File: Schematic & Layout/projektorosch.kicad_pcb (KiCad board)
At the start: 2 copper layers, 39 parts, among them J1 Power barrel plug, J2 RJ12, U1 ATmega328-P, U2 MAX232, Y1 Crystal

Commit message: design pcb - first try
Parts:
- removed C1: 100nF, Capacitor_SMD:C_0805_2012Metric_Pad1.18x1.45mm_HandSolder
- removed R12: R, Resistor_SMD:R_0805_2012Metric_Pad1.20x1.40mm_HandSolder
- removed RESET1: SW_SPST, Button_Switch_SMD:SW_Push_1P1T_NO_6x6mm_H9.5mm
- D2: footprint Diode_SMD:D_0805_2012Metric_Pad1.15x1.40mm_HandSolder -> Diode_THT:D_DO-15_P2.54mm_Vertical_KathodeUp
- moved BTN2 123.6 mm to (120.0, 140.0)
- moved BTN1 117.9 mm to (120.0, 110.0)
- moved R3 100.7 mm to (130.0, 139.0), turned to -90 degrees
- moved J1 95.0 mm to (194.0, 103.0), turned to 180 degrees
- moved R6 86.0 mm to (113.2, 131.0), turned to 90 degrees
- moved R7 85.5 mm to (135.0, 139.0), turned to -90 degrees
- moved R1 83.3 mm to (129.0, 106.0), turned to 180 degrees
- moved R2 73.8 mm to (133.0, 111.0), turned to 90 degrees
- moved R10 69.8 mm to (162.0, 139.0), turned to -90 degrees
- moved R11 68.8 mm to (157.0, 139.0), turned to -90 degrees
- moved BTN4 68.4 mm to (170.2, 140.0)
- moved C9 67.8 mm to (153.3, 130.0), turned to 180 degrees
- moved R14 67.7 mm to (193.0, 131.5), turned to 90 degrees
- moved F1 66.7 mm to (187.4, 114.2), turned to 0 degrees
- moved C7 61.7 mm to (180.3, 102.5), turned to 0 degrees
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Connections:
- J2 pad 1: /RX -> GND
- J2 pad 3: GND -> /RX
- J2 pad 5: /RTS -> /CTS
- J2 pad 6: /CTS -> /RTS
- U1 pad 12: unconnected-(U1-Pad12) -> BTN1
- U1 pad 2: /TX -> Net-(U1-Pad2)
- U1 pad 21: Net-(C1-Pad1) -> unconnected-(U1-Pad21)
- U1 pad 23: BTN1 -> unconnected-(U1-Pad23)
- U1 pad 25: BTN3 -> unconnected-(U1-Pad25)
- U1 pad 28: unconnected-(U1-Pad28) -> Net-(D2-Pad2)
- U1 pad 6: Net-(D2-Pad2) -> BTN3
- U2 pad 12: /TX -> Net-(U1-Pad2)
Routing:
- net VCC: track 0.00 -> 310.1 mm, vias 0 -> 6
- net GND: track 0.00 -> 267.3 mm, vias 0 -> 8
- net Net-(D2-Pad2): track 0.00 -> 97.4 mm, vias 0 -> 1
- net /RTS: track 0.00 -> 64.3 mm
- net /CTS: track 0.00 -> 61.7 mm
- net /TX: track 0.00 -> 61.0 mm, vias 0 -> 1
- net /RX: track 0.00 -> 57.4 mm
- net !RESET: track 0.00 -> 32.5 mm, vias 0 -> 2
- net BTN4: track 0.00 -> 31.6 mm
- net BTN3: track 0.00 -> 26.2 mm
- net Net-(R6-Pad1): track 0.00 -> 24.6 mm
- net Net-(BTN1-Pad1): track 0.00 -> 20.4 mm
- net Net-(BTN2-Pad1): track 0.00 -> 19.9 mm
- net Net-(C8-Pad2): track 0.00 -> 19.1 mm
- net Net-(R4-Pad1): track 0.00 -> 18.1 mm
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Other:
- board outline added: 100 x 63 mm

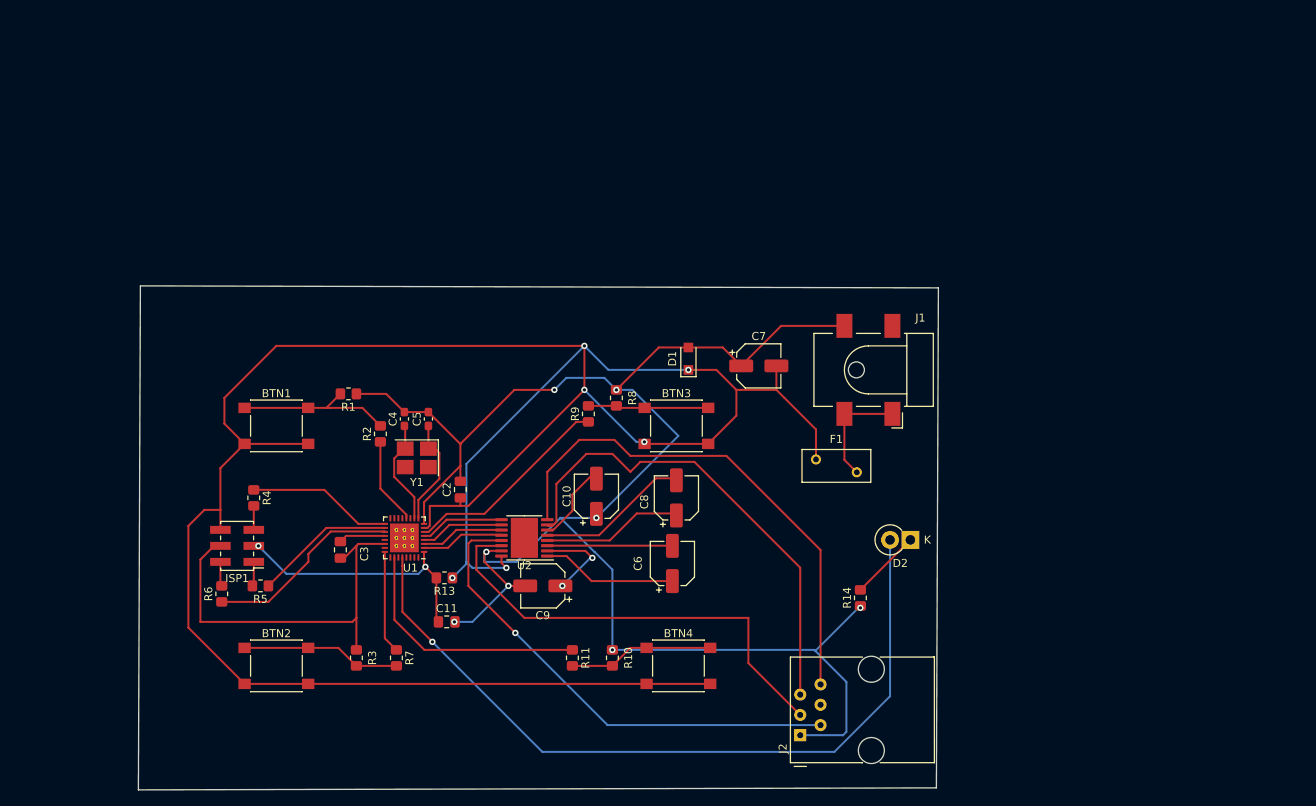
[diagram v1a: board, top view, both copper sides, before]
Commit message: redesign layout for attiny3216
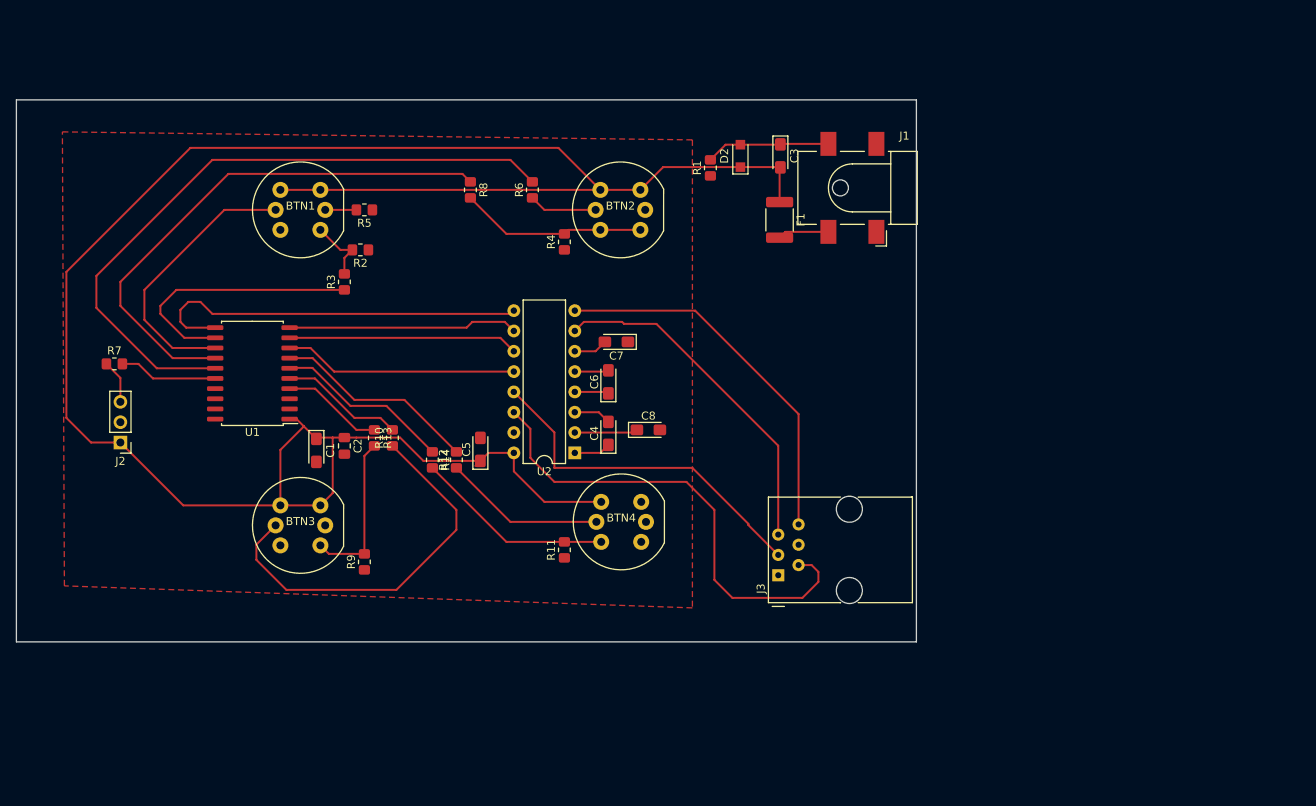
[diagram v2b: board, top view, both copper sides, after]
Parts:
- removed C10, C9: 10 uF, Capacitor_SMD:CP_Elec_5x5.7
- removed C11: 100nF, Capacitor_SMD:C_0805_2012Metric_Pad1.18x1.45mm_HandSolder
- removed D1: D_Zener 5.6V, Diode_SMD:Nexperia_CFP3_SOD-123W
- removed ISP1: Conn_02x03_Counter_Clockwise, Connector_PinHeader_2.00mm:PinHeader_2x03_P2.00mm_Vertical_SMD
- removed Y1: Crystal, Crystal:Crystal_SMD_3225-4Pin_3.2x2.5mm_HandSoldering
- added C1: 1u, Capacitor_Tantalum_SMD:CP_EIA-3216-10_Kemet-I_Pad1.58x1.35mm_HandSolder, F.Cu at (125.0, 113.1)
- added J3: RJ12, Connector_RJ:RJ12_Amphenol_54601, F.Cu at (182.7, 128.7)
- added R12: 220R, Resistor_SMD:R_0805_2012Metric_Pad1.20x1.40mm_HandSolder, F.Cu at (142.5, 114.2)
- BTN1: value ON_BTN -> LEDBTN; footprint Button_Switch_SMD:SW_Push_1P1T_NO_6x6mm_H9.5mm -> ledbtn_footprint:LBTN
- BTN2: value OFF_BTN -> LEDBTN; footprint Button_Switch_SMD:SW_Push_1P1T_NO_6x6mm_H9.5mm -> ledbtn_footprint:LBTN
- BTN3: value HDMI_BTN -> LEDBTN; footprint Button_Switch_SMD:SW_Push_1P1T_NO_6x6mm_H9.5mm -> ledbtn_footprint:LBTN
- BTN4: value VGA_BTN -> LEDBTN; footprint Button_Switch_SMD:SW_Push_1P1T_NO_6x6mm_H9.5mm -> ledbtn_footprint:LBTN
- C3: value 100n -> 10uF; footprint Capacitor_SMD:C_0805_2012Metric_Pad1.18x1.45mm_HandSolder -> Capacitor_Tantalum_SMD:CP_EIA-3216-12_Kemet-S_Pad1.58x1.35mm_HandSolder
- C4, C5: value 18p -> 1u; footprint Capacitor_SMD:C_0603_1608Metric_Pad1.08x0.95mm_HandSolder -> Capacitor_Tantalum_SMD:CP_EIA-3216-10_Kemet-I_Pad1.58x1.35mm_HandSolder
- C6, C8: value 10 uF -> 1u; footprint Capacitor_SMD:CP_Elec_5x5.7 -> Capacitor_Tantalum_SMD:CP_EIA-3216-10_Kemet-I_Pad1.58x1.35mm_HandSolder
- C7: value 10uF -> 1u; footprint Capacitor_SMD:CP_Elec_5x5.7 -> Capacitor_Tantalum_SMD:CP_EIA-3216-10_Kemet-I_Pad1.58x1.35mm_HandSolder
- D2: value LED -> D_Zener 5.6V; footprint Diode_THT:D_DO-15_P2.54mm_Vertical_KathodeUp -> Diode_SMD:Nexperia_CFP3_SOD-123W
- F1: footprint Fuse:Fuse_BelFuse_0ZRE0005FF_L8.3mm_W3.8mm -> Fuse:Fuse_1812_4532Metric_Pad1.30x3.40mm_HandSolder
- J2: value RJ12 -> Conn_01x03; footprint Connector_RJ:RJ12_Amphenol_54601 -> Connector_PinHeader_2.54mm:PinHeader_1x03_P2.54mm_Vertical
- R1: value 10K -> 0R
- R10: value 10K -> 220R
- R11, R2, R4, R9: value 100R -> 10K
- R13: value R -> 100R
- R14: value 220R -> 100R
- R3, R8: value 10K -> 100R
- R5, R6: value 100R -> 220R
- R7: value 100R -> 470R
- U1: value ATmega328-P -> ATtiny3216-S; footprint Package_DFN_QFN:QFN-32-1EP_5x5mm_P0.5mm_EP3.6x3.6mm_ThermalVias -> Package_SO:SOIC-20W_7.5x12.8mm_P1.27mm
- U2: footprint Package_SO:HTSSOP-16-1EP_4.4x5mm_P0.65mm_EP3.4x5mm_Mask2.46x2.31mm -> Package_DIP:DIP-16_W7.62mm
- moved J2 92.5 mm to (100.5, 112.1), turned to 180 degrees
- moved C3 73.8 mm to (183.0, 76.2)
- moved BTN2 71.4 mm to (163.0, 83.0)
- moved R6 63.7 mm to (152.0, 80.5)
- moved R14 56.2 mm to (139.5, 114.2), turned to -90 degrees
- moved R1 53.3 mm to (174.2, 77.8), turned to 90 degrees
- moved D2 52.5 mm to (178.0, 76.2), turned to 90 degrees
- moved R7 50.9 mm to (99.8, 102.2), turned to 0 degrees
- moved R4 50.3 mm to (156.0, 87.0), turned to 90 degrees
- moved R5 48.8 mm to (131.0, 83.0)
- moved BTN3 48.6 mm to (123.0, 122.4)
- moved R3 47.0 mm to (128.5, 92.0), turned to 90 degrees
- moved R10 38.9 mm to (134.5, 111.5), turned to 90 degrees
- moved R9 33.6 mm to (131.0, 127.0)
- moved R8 31.8 mm to (144.2, 80.5)
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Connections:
- BTN1 pad 1: Net-(BTN1-Pad1) -> VCC
- BTN1 pad 2: VCC -> Net-(BTN1-Pad2)
- BTN2 pad 1: Net-(BTN2-Pad1) -> VCC
- BTN2 pad 2: VCC -> Net-(BTN2-Pad2)
- BTN3 pad 1: Net-(BTN3-Pad1) -> VCC
- BTN3 pad 2: VCC -> Net-(BTN3-Pad2)
- BTN4 pad 1: Net-(BTN4-Pad1) -> VCC
- BTN4 pad 2: VCC -> Net-(BTN4-Pad2)
- C3 pad 1: VCC -> GND
- C3 pad 2: GND -> VCC
- C4 pad 2: GND -> Net-(C4-Pad2)
- C5 pad 1: Net-(C5-Pad1) -> VCC
- C7 pad 2: VCC -> Net-(C7-Pad2)
- C8 pad 2: Net-(C8-Pad2) -> GND
- D2 pad 1: Net-(D2-Pad1) -> VCC
- D2 pad 2: Net-(D2-Pad2) -> GND
- J2 pad 1: GND -> VCC
- J2 pad 2: /TX -> GND
- J2 pad 3: /RX -> Net-(J2-Pad3)
- R1 pad 2: Net-(BTN1-Pad1) -> GND
- R10 pad 1: GND -> Net-(BTN3-Pad3)
- R10 pad 2: Net-(BTN4-Pad1) -> BTN3LED
- R11 pad 1: BTN4 -> GND
- R11 pad 2: Net-(BTN4-Pad1) -> Net-(BTN4-Pad2)
- R13 pad 1: VCC -> BTN3
- R13 pad 2: !RESET -> Net-(BTN3-Pad2)
- R14 pad 1: GND -> BTN4
- R14 pad 2: Net-(D2-Pad1) -> Net-(BTN4-Pad2)
- R2 pad 1: BTN1 -> GND
- R2 pad 2: Net-(BTN1-Pad1) -> Net-(BTN1-Pad2)
- R3 pad 1: GND -> BTN1
- R3 pad 2: Net-(BTN2-Pad1) -> Net-(BTN1-Pad2)
- R4 pad 1: Net-(R4-Pad1) -> GND
- R4 pad 2: MOSI -> Net-(BTN2-Pad2)
- R5 pad 1: Net-(R5-Pad1) -> GND
- R5 pad 2: MISO -> Net-(BTN1-Pad4)
- R6 pad 1: Net-(R6-Pad1) -> Net-(BTN2-Pad3)
- R6 pad 2: SCK -> BTN2LED
- R7 pad 1: BTN2 -> Net-(J2-Pad3)
- R7 pad 2: Net-(BTN2-Pad1) -> UPDI
- R8 pad 1: GND -> BTN2
- R8 pad 2: Net-(BTN3-Pad1) -> Net-(BTN2-Pad2)
- R9 pad 1: BTN3 -> GND
- R9 pad 2: Net-(BTN3-Pad1) -> Net-(BTN3-Pad2)
- U1 pad 1: !RESET -> VCC
- U1 pad 10: Net-(C4-Pad1) -> CTSD
- U1 pad 11: unconnected-(U1-Pad11) -> RTSD
- U1 pad 13: unconnected-(U1-Pad13) -> BTN1LED
- U1 pad 14: unconnected-(U1-Pad14) -> BTN2
- U1 pad 15: unconnected-(U1-Pad15) -> BTN2LED
- U1 pad 16: unconnected-(U1-Pad16) -> UPDI
- U1 pad 17: Net-(R4-Pad1) -> unconnected-(U1-Pad17)
- U1 pad 18: Net-(R5-Pad1) -> unconnected-(U1-Pad18)
- U1 pad 19: Net-(R6-Pad1) -> unconnected-(U1-Pad19)
- U1 pad 2: Net-(U1-Pad2) -> unconnected-(U1-Pad2)
- U1 pad 20: VCC -> GND
- U1 pad 3: Net-(U1-Pad3) -> unconnected-(U1-Pad3)
- U1 pad 4: Net-(U1-Pad4) -> BTN3
- U1 pad 5: Net-(U1-Pad5) -> BTN3LED
- U1 pad 6: BTN3 -> BTN4
- U1 pad 7: VCC -> BTN4LED
- U1 pad 8: GND -> RXD
- U1 pad 9: Net-(C5-Pad1) -> TXD
- U2 pad 1: Net-(C6-Pad1) -> Net-(C4-Pad1)
- U2 pad 10: Net-(U1-Pad4) -> CTSD
- U2 pad 11: Net-(U1-Pad3) -> TXD
- U2 pad 12: Net-(U1-Pad2) -> RXD
- U2 pad 13: /TX -> RX
- U2 pad 14: /RX -> TX
- U2 pad 2: Net-(C9-Pad1) -> Net-(C8-Pad1)
- U2 pad 3: Net-(C6-Pad2) -> Net-(C4-Pad2)
- U2 pad 4: Net-(C8-Pad1) -> Net-(C6-Pad1)
- U2 pad 5: Net-(C8-Pad2) -> Net-(C6-Pad2)
- U2 pad 6: Net-(C10-Pad2) -> Net-(C7-Pad2)
- U2 pad 7: /CTS -> CTS
- U2 pad 8: /RTS -> RTS
- U2 pad 9: Net-(U1-Pad5) -> RTSD
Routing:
- net GND: track 267.3 -> 15.6 mm, vias 8 -> 0
- net Net-(D2-Pad2): track 97.4 -> 0.00 mm, vias 1 -> 0
- net BTN2LED: track 0.00 -> 83.6 mm
- net /RTS: track 64.3 -> 0.00 mm
- net /CTS: track 61.7 -> 0.00 mm
- net /TX: track 61.0 -> 0.00 mm, vias 1 -> 0
- net TX: track 0.00 -> 59.8 mm
- net /RX: track 57.4 -> 0.00 mm
- net BTN2: track 12.9 -> 67.3 mm
- net RTSD: track 0.00 -> 49.0 mm
- net Net-(BTN3-Pad3): track 0.00 -> 48.8 mm
- net RTS: track 0.00 -> 47.1 mm
- net VCC: track 310.1 -> 265.2 mm, vias 6 -> 0
- net RX: track 0.00 -> 44.2 mm
- net CTS: track 0.00 -> 43.4 mm
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- added copper zone on F.Cu, net GND
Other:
- board size 100 x 63 mm -> 112.5 x 67.8 mm

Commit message: attinty3216-remeljuk-final
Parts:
- removed D2: D_Zener 5.6V, Diode_SMD:Nexperia_CFP3_SOD-123W
- removed R1: 0R, Resistor_SMD:R_0805_2012Metric_Pad1.20x1.40mm_HandSolder
- removed R11, R4: 10K, Resistor_SMD:R_0805_2012Metric_Pad1.20x1.40mm_HandSolder
- removed R12, R6: 220R, Resistor_SMD:R_0805_2012Metric_Pad1.20x1.40mm_HandSolder
- removed R13, R14, R3: 100R, Resistor_SMD:R_0805_2012Metric_Pad1.20x1.40mm_HandSolder
- removed R7: 470R, Resistor_SMD:R_0805_2012Metric_Pad1.20x1.40mm_HandSolder
- added D1: D_Zener 5.6V, Diode_SMD:Nexperia_CFP3_SOD-123W, F.Cu at (176.8, 78.7)
- J1: value Power barrel plug -> Barrel_Jack_Switch; footprint Connector_BarrelJack:BarrelJack_CLIFF_FC681465S_SMT_Horizontal -> Connector_BarrelJack:BarrelJack_Horizontal
- R2, R9: value 10K -> 220R
- R8: value 100R -> 470R
- moved R8 31.5 mm to (123.1, 103.8), turned to 0 degrees
- moved R2 24.4 mm to (154.2, 82.3)
- moved C8 24.0 mm to (153.5, 90.3), turned to 90 degrees
- moved R5 20.1 mm to (123.1, 101.5), turned to 0 degrees
- moved J2 18.6 mm to (118.9, 109.0)
- moved R9 17.3 mm to (124.8, 110.9)
- moved U1 16.1 mm to (133.1, 103.3)
- moved R10 12.6 mm to (146.6, 107.7)
- moved C7 11.0 mm to (156.5, 90.3), turned to -90 degrees
- moved C3 9.47 mm to (173.9, 78.7), turned to 90 degrees
- moved C1 8.84 mm to (133.7, 114.7), turned to 180 degrees
- moved J1 6.00 mm to (186.0, 79.7)
- moved F1 5.81 mm to (180.7, 78.9)
- moved C2 5.62 mm to (134.1, 111.9), turned to 180 degrees
- moved C5 1.32 mm to (146.6, 112.1)
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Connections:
- BTN1 pad 1: VCC -> GND
- BTN1 pad 2: Net-(BTN1-Pad2) -> BTN1
- BTN1 pad 3: BTN1LED -> Net-(BTN1-Pad3)
- BTN1 pad 4: Net-(BTN1-Pad4) -> GND
- BTN2 pad 1: VCC -> GND
- BTN2 pad 2: Net-(BTN2-Pad2) -> BTN2
- BTN3 pad 1: VCC -> GND
- BTN3 pad 2: Net-(BTN3-Pad2) -> BTN3
- BTN4 pad 1: VCC -> GND
- BTN4 pad 2: Net-(BTN4-Pad2) -> BTN4
- J1 pad 3: (no net) -> GND
- R10 pad 1: Net-(BTN3-Pad3) -> Net-(BTN4-Pad3)
- R10 pad 2: BTN3LED -> BTN4LED
- R2 pad 1: GND -> Net-(BTN2-Pad3)
- R2 pad 2: Net-(BTN1-Pad2) -> BTN2LED
- R5 pad 1: GND -> Net-(BTN1-Pad3)
- R5 pad 2: Net-(BTN1-Pad4) -> BTN1LED
- R8 pad 1: BTN2 -> Net-(J2-Pad3)
- R8 pad 2: Net-(BTN2-Pad2) -> UPDI
- R9 pad 1: GND -> Net-(BTN3-Pad3)
- R9 pad 2: Net-(BTN3-Pad2) -> BTN3LED
- U1 pad 12: BTN1 -> BTN2
- U1 pad 13: BTN1LED -> BTN2LED
- U1 pad 14: BTN2 -> BTN1
- U1 pad 15: BTN2LED -> BTN1LED
- U1 pad 17: unconnected-(U1-Pad17) -> BTN3
- U1 pad 18: unconnected-(U1-Pad18) -> BTN3LED
- U1 pad 2: unconnected-(U1-Pad2) -> BTN4
- U1 pad 3: unconnected-(U1-Pad3) -> GND
- U1 pad 4: BTN3 -> GND
- U1 pad 5: BTN3LED -> BTN4LED
- U1 pad 6: BTN4 -> unconnected-(U1-Pad6)
- U1 pad 7: BTN4LED -> unconnected-(U1-Pad7)
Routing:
- net VCC: track 265.2 -> 177.1 mm
- net BTN2LED: track 83.6 -> 39.3 mm
- net Net-(BTN3-Pad3): track 48.8 -> 13.2 mm
- net BTN1LED: track 34.6 -> 4.90 mm
- net RTSD: track 49.0 -> 22.0 mm
- net Net-(BTN4-Pad2): track 24.9 -> 0.00 mm
- net Net-(BTN2-Pad2): track 23.3 -> 0.00 mm
- net BTN2: track 67.3 -> 46.8 mm
- net Net-(BTN1-Pad3): track 0.00 -> 20.3 mm
- net Net-(BTN3-Pad2): track 20.0 -> 0.00 mm
- net BTN3: track 12.7 -> 32.6 mm
- net CTSD: track 28.8 -> 12.2 mm
- net RXD: track 29.3 -> 13.2 mm
- net TXD: track 28.7 -> 12.7 mm
- net BTN4LED: track 25.7 -> 9.98 mm
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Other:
- board size 112.5 x 67.8 mm -> 92.3 x 67.8 mm

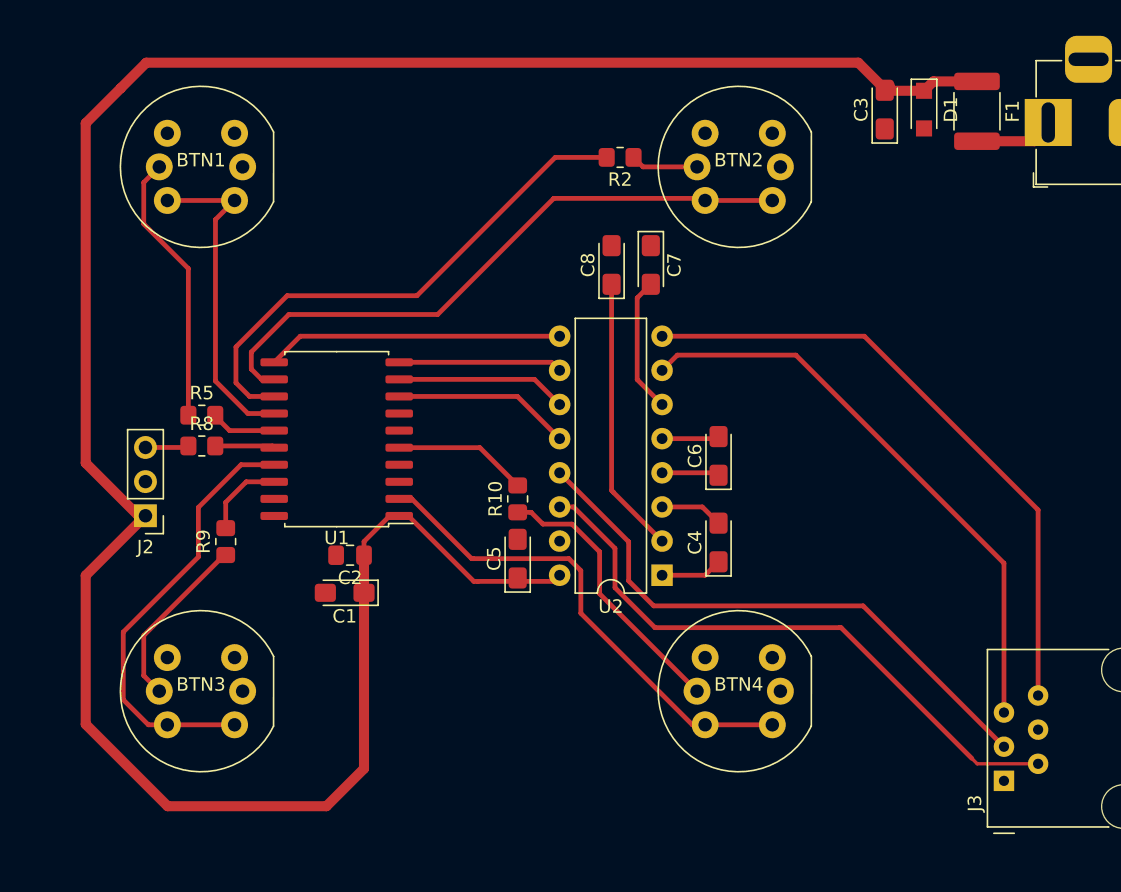
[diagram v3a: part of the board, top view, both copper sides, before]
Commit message: attiny214 - the right files
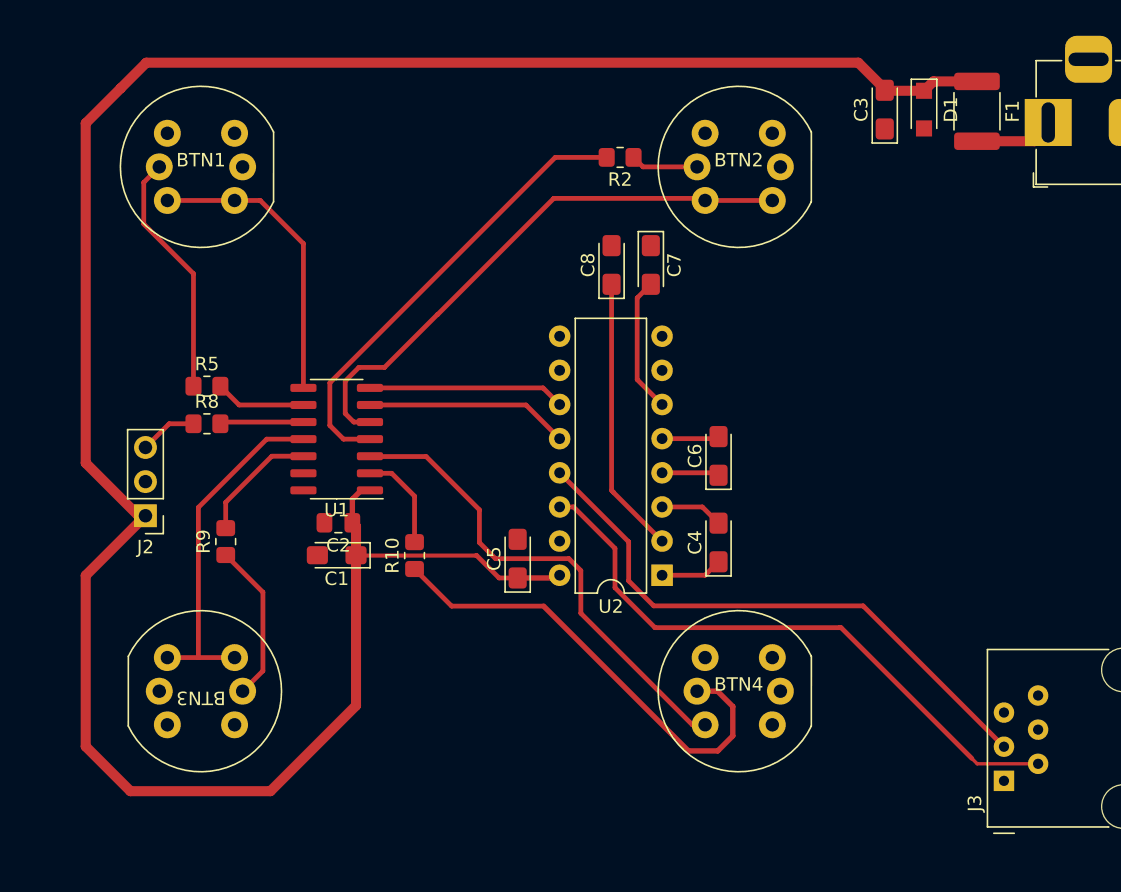
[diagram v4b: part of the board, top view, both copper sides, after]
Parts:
- U1: value ATtiny3216-S -> ATtiny214-SS; footprint Package_SO:SOIC-20W_7.5x12.8mm_P1.27mm -> Package_SO:SOIC-14_3.9x8.7mm_P1.27mm
- moved R10 8.75 mm to (138.9, 111.9)
- moved C1 2.86 mm to (133.1, 111.9)
- moved C2 2.56 mm to (133.2, 109.5)
- moved R5 2.19 mm to (123.4, 99.3)
- moved R8 1.69 mm to (123.4, 102.1)
- turned BTN3 to 180 degrees
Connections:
- J3 pad 5: CTS -> unconnected-(J3-Pad5)
- J3 pad 6: RTS -> unconnected-(J3-Pad6)
- U1 pad 10: CTSD -> UPDI
- U1 pad 11: RTSD -> BTN3
- U1 pad 12: BTN2 -> BTN3LED
- U1 pad 13: BTN2LED -> unconnected-(U1-Pad13)
- U1 pad 14: BTN1 -> GND
- U1 pad 2: BTN4 -> BTN4LED
- U1 pad 3: GND -> BTN4
- U1 pad 4: GND -> BTN2LED
- U1 pad 5: BTN4LED -> BTN2
- U1 pad 6: unconnected-(U1-Pad6) -> RXD
- U1 pad 7: unconnected-(U1-Pad7) -> TXD
- U1 pad 8: RXD -> BTN1
- U1 pad 9: TXD -> BTN1LED
- U2 pad 10: CTSD -> unconnected-(U2-Pad10)
- U2 pad 7: CTS -> unconnected-(U2-Pad7)
- U2 pad 8: RTS -> unconnected-(U2-Pad8)
- U2 pad 9: RTSD -> unconnected-(U2-Pad9)
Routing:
- net RTS: track 47.1 -> 0.00 mm
- net CTS: track 43.4 -> 0.00 mm
- net RTSD: track 22.0 -> 0.00 mm
- net Net-(BTN4-Pad3): track 20.7 -> 35.1 mm
- net CTSD: track 12.2 -> 0.00 mm
- net BTN3: track 32.6 -> 26.1 mm
- net BTN2LED: track 39.3 -> 34.1 mm
- net BTN2: track 46.8 -> 42.0 mm
- net BTN3LED: track 6.16 -> 9.12 mm
- net BTN4LED: track 9.98 -> 7.44 mm
- net BTN1: track 24.4 -> 22.2 mm
- net Net-(BTN1-Pad3): track 20.3 -> 18.3 mm
- net TXD: track 12.7 -> 14.6 mm
- net RXD: track 13.2 -> 15.1 mm
- net BTN1LED: track 4.90 -> 6.76 mm
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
